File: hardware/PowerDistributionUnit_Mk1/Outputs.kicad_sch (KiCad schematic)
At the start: 13 parts, among them U25 NL17SZS11DFT2G-Q

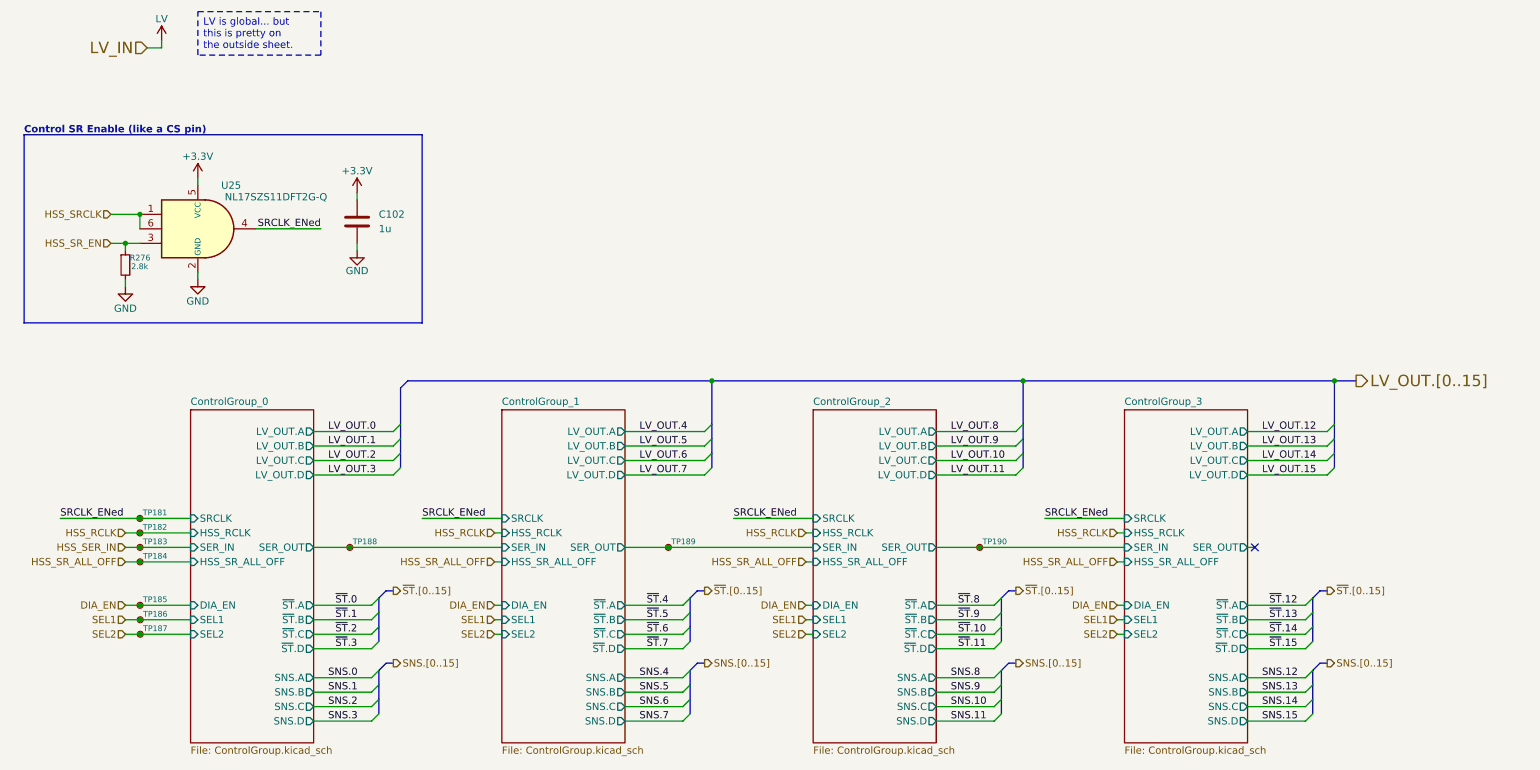
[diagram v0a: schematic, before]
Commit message: schematic updates (found switch, LED resistor values, LV sense ADC pin filter, removed unnecessary parallel resistors, switched to new SR), addressed review comments (input fuse, 3.3V LED, SPI naming fix)
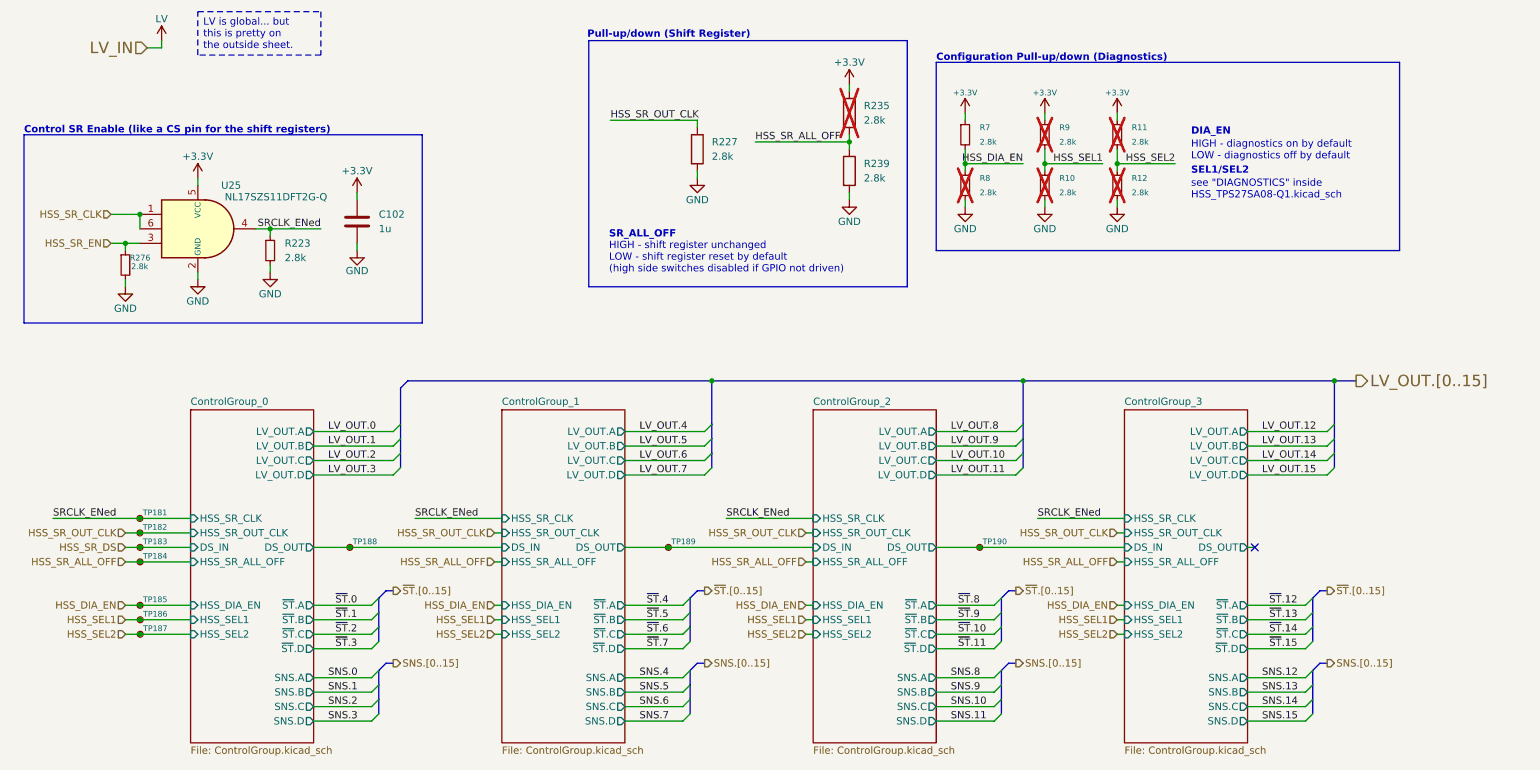
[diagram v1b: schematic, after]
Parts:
- added R10, R11, R12, R223, R7, R8, R9: 2.8k, Resistor_SMD:R_0603_1608Metric, symbol PowerDistributionUnitResistorLib:2.8k_Small
- added R227, R235, R239: 2.8k, Resistor_SMD:R_0603_1608Metric, symbol PowerDistributionUnitResistorLib:2.8k
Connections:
- net +3.3V: now also R11.1, R235.1, R7.1, R9.1
- net GND: now also R10.2, R12.2, R223.2, R227.2, R239.2, R8.2
- net HSS_SR_ALL_OFF: now also R235.2, R239.1
- net SRCLK_ENed: now also R223.1
- net ControlGroup_0/SER_OUT renamed ControlGroup_0/DS_OUT
- net ControlGroup_1/SER_OUT renamed ControlGroup_1/DS_OUT
- net ControlGroup_2/SER_OUT renamed ControlGroup_2/DS_OUT
- net DIA_EN renamed HSS_DIA_EN
- net HSS_DIA_EN: now also R7.2, R8.1
- net HSS_RCLK renamed HSS_SR_OUT_CLK
- net HSS_SR_OUT_CLK: now also R227.1
- net HSS_SER_IN renamed HSS_SR_DS
- net HSS_SRCLK renamed HSS_SR_CLK
- net SEL1 renamed HSS_SEL1
- net HSS_SEL1: now also R10.1, R9.2
- net SEL2 renamed HSS_SEL2
- net HSS_SEL2: now also R11.2, R12.1
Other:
- sheet ControlGroup_0 ports: added DS_IN, DS_OUT, HSS_DIA_EN, HSS_SEL1, HSS_SEL2, HSS_SR_CLK, HSS_SR_OUT_CLK; removed DIA_EN, HSS_RCLK, SEL1, SEL2, SER_IN, SER_OUT, SRCLK
- sheet ControlGroup_1 ports: added DS_IN, DS_OUT, HSS_DIA_EN, HSS_SEL1, HSS_SEL2, HSS_SR_CLK, HSS_SR_OUT_CLK; removed DIA_EN, HSS_RCLK, SEL1, SEL2, SER_IN, SER_OUT, SRCLK
- sheet ControlGroup_2 ports: added DS_IN, DS_OUT, HSS_DIA_EN, HSS_SEL1, HSS_SEL2, HSS_SR_CLK, HSS_SR_OUT_CLK; removed DIA_EN, HSS_RCLK, SEL1, SEL2, SER_IN, SER_OUT, SRCLK
- sheet ControlGroup_3 ports: added DS_IN, DS_OUT, HSS_DIA_EN, HSS_SEL1, HSS_SEL2, HSS_SR_CLK, HSS_SR_OUT_CLK; removed DIA_EN, HSS_RCLK, SEL1, SEL2, SER_IN, SER_OUT, SRCLK
- note added: "Configuration Pull-up/down (Diagnostics)"
- note added: "Control SR Enable (like a CS pin for the shift registers)"
- note added: "DIA_EN"
- note added: "HIGH - diagnostics on by default LOW - diagnostics off by default"
- note added: "HIGH - shift register unchanged LOW - shift register reset by default (high side switches disabled if GPIO not driven)"
- note added: "Pull-up/down (Shift Register)"
- note added: "SEL1/SEL2"
- note added: "SR_ALL_OFF"
- note added: "see "DIAGNOSTICS" inside HSS_TPS27SA08-Q1.kicad_sch"
- note removed: "Control SR Enable (like a CS pin)"

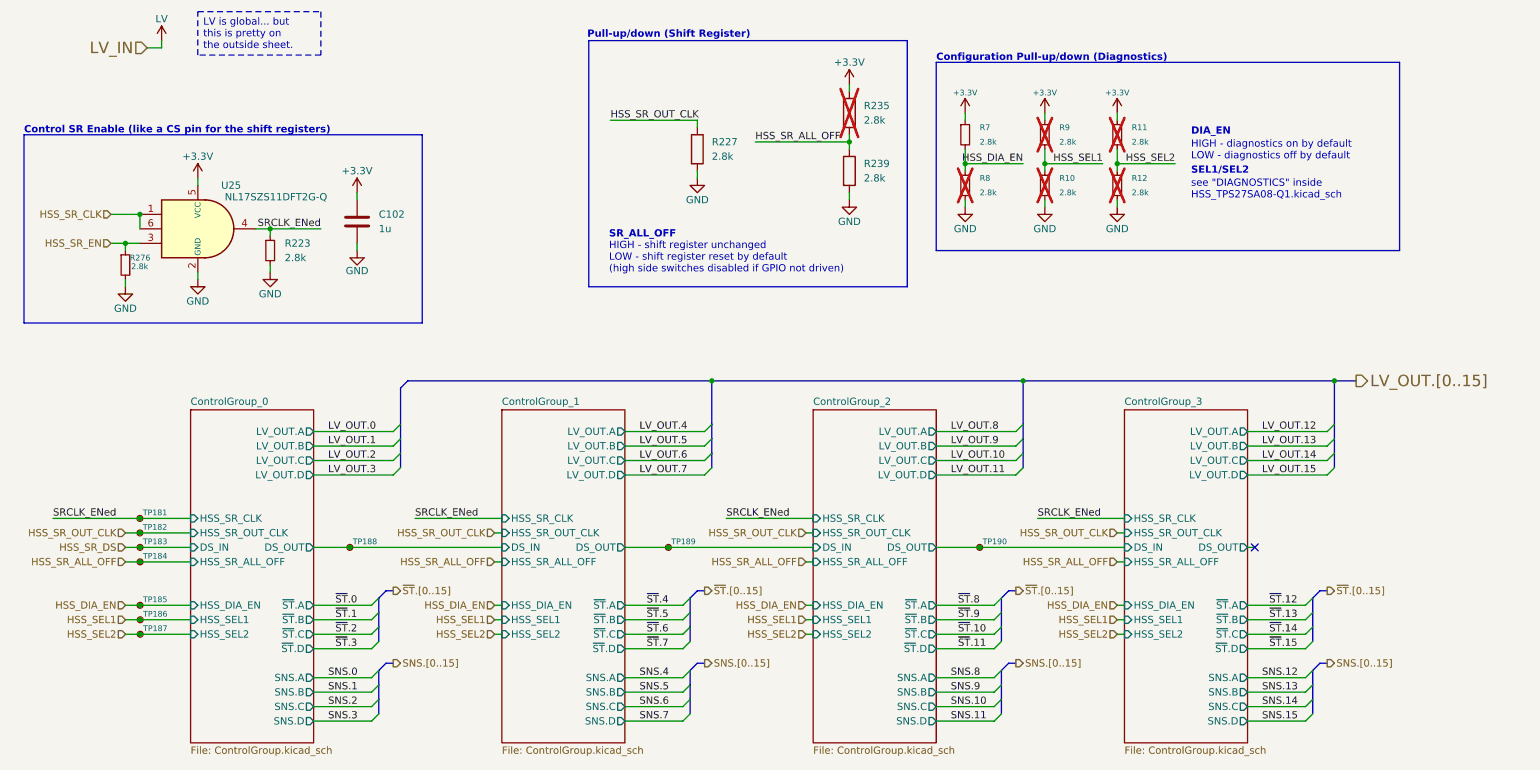
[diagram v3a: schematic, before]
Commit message: BBPDU Mk1 RevB (#6)
* update adc reference to use internal reference (open) with jumper option

* change ADC - reading voltage to resistor divider with option to reference to GND or 1.65V

* change ADC AVDD and AGND connections to regular 3.3V and GND

* make input protection use b2b FETs

* update KiCad-Sharepoint

* update LeaderSOM symbol and SPI pinout (bottom) - need to swap SPI2 and SPI3 names, remove local library copy of LeaderSOM symbol

* change LSOM footprint to centered LSOM footprint, make centered LSOM footprint plated to address hidden pins on LSOM symbol

* update PCB from schematic

* layout/routing for input protection

* fix centered LSOM footprint 3D model, update footprint

* reroute LSOM SPI connections, repin logic analyzer connections

* reroute updated AVDD and AGND on ADCs

* reroute ADCIN- connections to resistor divider from 3.3VA (for 1.65V or 0V)

* change jumper to DNP resistor for ADC reference, routed

* route a couple of missed connections (LV in connection to input prot IC, LV sense connection)

* address DRC

* fix silkscreen labelling issues

* add SRCLK_ENed connection to logic analyzer connector

* silkscreen fixes and stuff

* update rev and year label

* address DRC

* update schematic documentation, clean up, update titleblocks

* add LCSC P/N to libs

* update all symbols with LCSC P/N

* update PCB with LCSC P/Ns

* add center mounting hole

* correct SR part number to SOIC package

* correct fuse table

* change lv sense rdiv values to avoid extended components, update all pull-ups/-downs using 2.8k

* rotate nanofits for inwards clip

* NC the mounting holes (because Lakshay Gupta)

* fix shorted nets error from wrong size res symbol from resistor change

* address DRC

* assembly setup, change latch pull resistor DNP to latch off instead of auto retry by default

* silkscreen stuff

* change DNP for HSS diagnostics to default to current

* change DNP to disable HSS diagnostics by default (primarily use external current 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
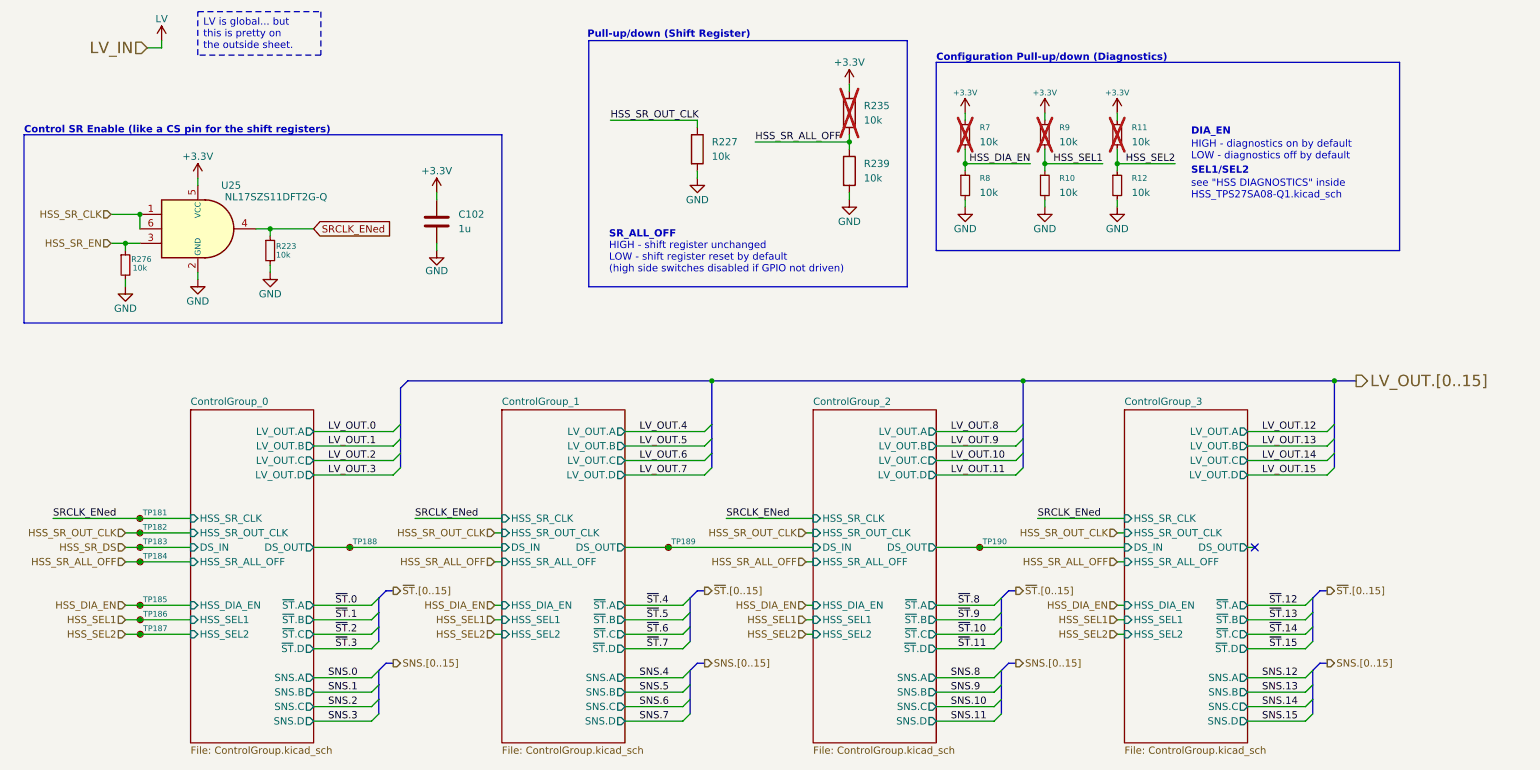
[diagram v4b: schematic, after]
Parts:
- C102: LCSC P/N (none) -> C15849
- R10, R12, R8: value 2.8k -> 10k; symbol PowerDistributionUnitResistorLib:2.8k_Small -> PowerDistributionUnitResistorLib:10k_Small; LCSC P/N (none) -> C25804; Mouser P/N 71-CRCW0603-2.8K-E3 -> 71-CRCW060310K0FKEI; P/N CRCW06032K80FKEA -> CRCW060310K0FKEI; now fitted
- R11, R223, R276, R9: value 2.8k -> 10k; symbol PowerDistributionUnitResistorLib:2.8k_Small -> PowerDistributionUnitResistorLib:10k_Small; LCSC P/N (none) -> C25804; Mouser P/N 71-CRCW0603-2.8K-E3 -> 71-CRCW060310K0FKEI; P/N CRCW06032K80FKEA -> CRCW060310K0FKEI
- R227, R235, R239: value 2.8k -> 10k; symbol PowerDistributionUnitResistorLib:2.8k -> PowerDistributionUnitResistorLib:10k; LCSC P/N (none) -> C25804; Mouser P/N 71-CRCW0603-2.8K-E3 -> 71-CRCW060310K0FKEI; P/N CRCW06032K80FKEA -> CRCW060310K0FKEI
- R7: value 2.8k -> 10k; symbol PowerDistributionUnitResistorLib:2.8k_Small -> PowerDistributionUnitResistorLib:10k_Small; LCSC P/N (none) -> C25804; Mouser P/N 71-CRCW0603-2.8K-E3 -> 71-CRCW060310K0FKEI; P/N CRCW06032K80FKEA -> CRCW060310K0FKEI; now not fitted
- U25: LCSC P/N (none) -> C23078196
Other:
- note added: "see "HSS DIAGNOSTICS" inside HSS_TPS27SA08-Q1.kicad_sch"
- note removed: "see "DIAGNOSTICS" inside HSS_TPS27SA08-Q1.kicad_sch"
- moved on the sheet: C102
